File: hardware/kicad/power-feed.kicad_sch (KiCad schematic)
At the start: 0 parts

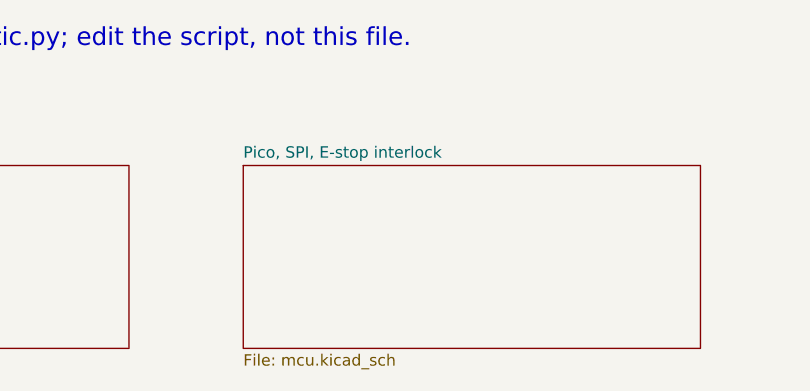
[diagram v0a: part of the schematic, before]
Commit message: Schematic: bare RP2040 instead of the Pico module
RP2040 (QFN-56) per Raspberry Pi's minimal design: W25Q16JV 2 MB QSPI flash, 12 MHz crystal with 1k series,
internal 1.1 V core regulator, BOOTSEL + RESET buttons, JST-SH SWD, status LED on GPIO25, USB-C (5.1k CC,
27R series). +3V3 now from an AP2112K-3.3 fed by VSYS = +5V or USB VBUS through Schottkys. Same GPIO
numbers as the Pico, so the firmware is unchanged. ERC 0 findings, netlist 132 nets / 189 parts match.
Layout follows (PCB agent). LCSC numbers for the flash and crystal still to be verified.

Co-Authored-By: Claude Opus 5.5 <noreply@anthropic.com>
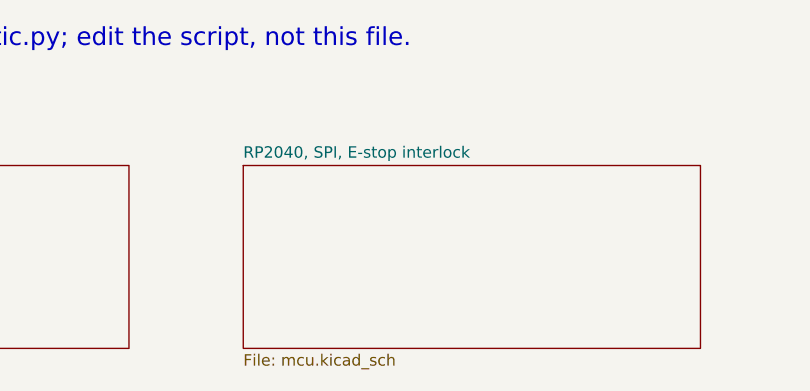
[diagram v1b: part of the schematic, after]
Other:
- sheet Pico, SPI, E-stop interlock renamed RP2040, SPI, E-stop interlock
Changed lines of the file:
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@@
 			(color 0 0 0 0)
 		)
-		(property "Sheetname" "Pico, SPI, E-stop interlock"
+		(property "Sheetname" "RP2040, SPI, E-stop interlock"
 			(at 152.4 39.9284 0)
 			(effects
